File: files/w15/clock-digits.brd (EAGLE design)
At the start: 100 x 80 mm, 6 parts, among them IC1 ATTINY44-SSU, IC2 5V

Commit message: board routing
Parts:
- added R10, R11, R12, R13, R14, R15, R2, R3, R4, R5, R6, R7, R8, R9: (no value), fab:R1206FAB
- added U$10, U$11, U$12, U$13, U$14, U$15, U$16, U$3, U$4, U$5, U$6, U$7, U$8, U$9: LEDFAB1206, fab:LED1206FAB
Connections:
- new net N$1: IC1.13, R2.1, R9.1
- new net N$10: R6.1, U$11.1
- new net N$11: IC1.2, R14.2, R7.2
- new net N$12: R7.1, U$12.1
- new net N$14: R8.1, U$6.1
- new net N$15: IC1.5, R15.2, U$10.2, U$11.2, U$12.2, U$3.2, U$4.2, U$5.2, U$6.2
- new net N$16: R9.2, U$7.1
- new net N$17: R15.1, U$16.1
- new net N$18: R10.1, U$8.1
- new net N$2: R2.2, U$3.1
- new net N$20: R11.1, U$9.1
- new net N$21: R12.1, U$13.1
- new net N$23: R13.1, U$14.1
- new net N$24: R14.1, U$15.1
- new net N$28: IC1.3, R8.2, U$13.2, U$14.2, U$15.2, U$16.2, U$7.2, U$8.2, U$9.2
- new net N$3: IC1.12, R10.2, R3.2
- new net N$4: R3.1, U$4.1
- new net N$5: IC1.11, R11.2, R4.2
- new net N$6: R4.1, U$5.1
- new net N$7: IC1.10, R12.2, R5.2
- new net N$8: R5.1, U$10.1
- new net N$9: IC1.6, R13.2, R6.2
- net SCK: now also IC1.9
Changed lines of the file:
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@@
 <element name="U$1" library="fab" package="2X03SMD" value="AVRISPSMD" x="16.51" y="24.13"/>
 <element name="U$2" library="fab" package="2X02SMD" value="PINHD-2X2-SMD" x="33.02" y="38.1" rot="R180"/>
+<element name="R2" library="fab" package="R1206FAB" value="" x="44.45" y="52.07"/>
+<element name="U$3" library="fab" package="LED1206FAB" value="LEDFAB1206" x="52.07" y="44.45"/>
+<element name="U$4" library="fab" package="LED1206FAB" value="LEDFAB1206" x="57.15" y="38.1" rot="R90"/>
+<element name="U$5" library="fab" package="LED1206FAB" value="LEDFAB1206" x="57.15" y="27.94" rot="R90"/>
+<element name="R3" library="fab" package="R1206FAB" value="" x="53.34" y="49.53"/>
+<element name="R4" library="fab" package="R1206FAB" value="" x="60.96" y="48.26"/>
+<element name="R5" library="fab" package="R1206FAB" value="" x="52.07" y="15.24"/>
+<element name="U$10" library="fab" package="LED1206FAB" value="LEDFAB1206" x="52.07" y="22.86"/>
+<element name="R6" library="fab" package="R1206FAB" value="" x="40.64" y="27.94"/>
+<element name="U$11" library="fab" package="LED1206FAB" value="LEDFAB1206" x="46.99" y="27.94" rot="R90"/>
+<element name="R7" library="fab" package="R1206FAB" value="" x="40.64" y="38.1"/>
+<element name="U$12" library="fab" package="LED1206FAB" value="LEDFAB1206" x="46.99" y="38.1" rot="R90"/>
+<element name="R8" library="fab" package="R1206FAB" value="" x="62.23" y="33.02"/>
+<element name="U$6" library="fab" package="LED1206FAB" value="LEDFAB1206" x="52.07" y="33.02"/>
+<element name="R9" library="fab" package="R1206FAB" value="" x="71.12" y="52.07"/>
+<element name="U$7" library="fab" package="LED1206FAB" value="LEDFAB1206" x="77.47" y="44.45"/>
+<element name="U$8" library="fab" package="LED1206FAB" value="LEDFAB1206" x="82.55" y="38.1" rot="R90"/>
+<element name="U$9" library="fab" package="LED1206FAB" value="LEDFAB1206" x="82.55" y="27.94" rot="R90"/>
+<element name="R10" library="fab" package="R1206FAB" value="" x="81.28" y="49.53"/>
+<element name="R11" library="fab" package="R1206FAB" value="" x="90.17" y="48.26"/>
+<element name="R12" library="fab" package="R1206FAB" value="" x="77.47" y="15.24"/>
+<element name="U$13" library="fab" package="LED1206FAB" value="LEDFAB1206" x="77.47" y="22.86"/>
+<element name="R13" library="fab" package="R1206FAB" value="" x="64.77" y="27.94" rot="R180"/>
+<element name="U$14" library="fab" package="LED1206FAB" value="LEDFAB1206" x="72.39" y="27.94" rot="R90"/>
+<element name="R14" library="fab" package="R1206FAB" value="" x="64.77" y="38.1" rot="R180"/>
+<element name="U$15" library="fab" package="LED1206FAB" value="LEDFAB1206" x="72.39" y="38.1" rot="R90"/>
+<element name="R15" library="fab" package="R1206FAB" value="" x="69.85" y="33.02"/>
+<element name="U$16" library="fab" package="LED1206FAB" value="LEDFAB1206" x="77.47" y="33.02"/>
 </elements>
 <signals>
@@
 <signal name="SCK">
 <contactref element="U$1" pad="3"/>
+<contactref element="IC1" pad="9"/>
+<wire x1="13.97" y1="24.13" x2="33.0835" y2="21.59" width="0" layer="19" extent="1-1"/>
+</signal>
+<signal name="N$2">
+<contactref element="R2" pad="2"/>
+<contactref element="U$3" pad="1"/>
+<wire x1="46.101" y1="52.07" x2="50.419" y2="44.45" width="0" layer="19" extent="1-1"/>
+</signal>
+<signal name="N$3">
+<contactref element="IC1" pad="12"/>
+<contactref element="R3" pad="2"/>
+<contactref element="R10" pad="2"/>
+<wire x1="54.991" y1="49.53" x2="82.931" y2="49.53" width="0" layer="19" extent="1-1"/>
+<wire x1="33.0835" y1="25.4" x2="54.991" y2="49.53" width="0" layer="19" extent="1-1"/>
+</signal>
+<signal name="N$4">
+<contactref element="R3" pad="1"/>
+<contactref element="U$4" pad="1"/>
+<wire x1="57.15" y1="36.449" x2="51.689" y2="49.53" width="0" layer="19" extent="1-1"/>
+</signal>
+<signal name="N$5">
+<contactref element="IC1" pad="11"/>
+<contactref element="R4" pad="2"/>
+<contactref element="R11" pad="2"/>
+<wire x1="62.611" y1="48.26" x2="91.821" y2="48.26" width="0" layer="19" extent="1-1"/>
+<wire x1="33.0835" y1="24.13" x2="62.611" y2="48.26" width="0" layer="19" extent="1-1"/>
+</signal>
+<signal name="N$6">
+<contactref element="R4" pad="1"/>
+<contactref element="U$5" pad="1"/>
+<wire x1="57.15" y1="26.289" x2="59.309" y2="48.26" width="0" layer="19" extent="1-1"/>
+</signal>
+<signal name="N$8">
+<contactref element="R5" pad="1"/>
+<contactref element="U$10" pad="1"/>
+<wire x1="50.419" y1="15.24" x2="50.419" y2="22.86" width="0" layer="19" extent="1-1"/>
+</signal>
+<signal name="N$9">
+<contactref element="IC1" pad="6"/>
+<contactref element="R6" pad="2"/>
+<contactref element="R13" pad="2"/>
+<wire x1="42.291" y1="27.94" x2="63.119" y2="27.94" width="0" layer="19" extent="1-1"/>
+<wire x1="27.8765" y1="21.59" x2="42.291" y2="27.94" width="0" layer="19" extent="1-1"/>
+</signal>
+<signal name="N$10">
+<contactref element="R6" pad="1"/>
+<contactref element="U$11" pad="1"/>
+<wire x1="38.989" y1="27.94" x2="46.99" y2="26.289" width="0" layer="19" extent="1-1"/>
+</signal>
+<signal name="N$12">
+<contactref element="R7" pad="1"/>
+<contactref element="U$12" pad="1"/>
+<wire x1="38.989" y1="38.1" x2="46.99" y2="36.449" width="0" layer="19" extent="1-1"/>
+</signal>
+<signal name="N$14">
+<contactref element="R8" pad="1"/>
+<contactref element="U$6" pad="1"/>
+<wire x1="60.579" y1="33.02" x2="50.419" y2="33.02" width="0" layer="19" extent="1-1"/>
+</signal>
+<signal name="N$1">
+<contactref element="IC1" pad="13"/>
+<contactref element="R2" pad="1"/>
+<contactref element="R9" pad="1"/>
+<wire x1="42.799" y1="52.07" x2="69.469" y2="52.07" width="0" layer="19" extent="1-1"/>
+<wire x1="33.0835" y1="26.67" x2="42.799" y2="52.07" width="0" layer="19" extent="1-1"/>
+</signal>
+<signal name="N$7">
+<contactref element="IC1" pad="10"/>
+<contactref element="R5" pad="2"/>
+<contactref element="R12" pad="2"/>
+<wire x1="53.721" y1="15.24" x2="79.121" y2="15.24" width="0" layer="19" extent="1-1"/>
+<wire x1="33.0835" y1="22.86" x2="53.721" y2="15.24" width="0" layer="19" extent="1-1"/>
+</signal>
+<signal name="N$11">
+<contactref element="IC1" pad="2"/>
+<contactref element="R7" pad="2"/>
+<contactref element="R14" pad="2"/>
+<wire x1="42.291" y1="38.1" x2="63.119" y2="38.1" width="0" layer="19" extent="1-1"/>
+<wire x1="27.8765" y1="26.67" x2="42.291" y2="38.1" width="0" layer="19" extent="1-1"/>
+</signal>
+<signal name="N$15">
+<contactref element="IC1" pad="5"/>
+<contactref element="U$3" pad="2"/>
+<contactref element="U$4" pad="2"/>
+<contactref element="U$5" pad="2"/>
+<contactref element="U$10" pad="2"/>
+<contactref element="U$11" pad="2"/>
+<contactref element="U$12" pad="2"/>
+<contactref element="R15" pad="2"/>
+<contactref element="U$6" pad="2"/>
+<wire x1="53.721" y1="33.02" x2="71.501" y2="33.02" width="0" layer="19" extent="1-1"/>
+<wire x1="46.99" y1="39.751" x2="53.721" y2="33.02" width="0" layer="19" extent="1-1"/>
+<wire x1="46.99" y1="29.591" x2="46.99" y2="39.751" width="0" layer="19" extent="1-1"/>
+<wire x1="53.721" y1="22.86" x2="46.99" y2="29.591" width="0" layer="19" extent="1-1"/>
+<wire x1="57.15" y1="29.591" x2="53.721" y2="22.86" width="0" layer="19" extent="1-1"/>
+<wire x1="57.15" y1="39.751" x2="57.15" y2="29.591" width="0" layer="19" extent="1-1"/>
+<wire x1="53.721" y1="44.45" x2="57.15" y2="39.751" width="0" layer="19" extent="1-1"/>
+<wire x1="27.8765" y1="22.86" x2="53.721" y2="44.45" width="0" layer="19" extent="1-1"/>
+</signal>
+<signal name="N$16">
+<contactref element="R9" pad="2"/>
+<contactref element="U$7" pad="1"/>
+<wire x1="75.819" y1="44.45" x2="72.771" y2="52.07" width="0" layer="19" extent="1-1"/>
+</signal>
+<signal name="N$18">
+<contactref element="R10" pad="1"/>
+<contactref element="U$8" pad="1"/>
+<wire x1="82.55" y1="36.449" x2="79.629" y2="49.53" width="0" layer="19" extent="1-1"/>
+</signal>
+<signal name="N$20">
+<contactref element="R11" pad="1"/>
+<contactref element="U$9" pad="1"/>
+<wire x1="82.55" y1="26.289" x2="88.519" y2="48.26" width="0" layer="19" extent="1-1"/>
+</signal>
+<signal name="N$21">
+<contactref element="R12" pad="1"/>
+<contactref element="U$13" pad="1"/>
+<wire x1="75.819" y1="22.86" x2="75.819" y2="15.24" width="0" layer="19" extent="1-1"/>
+</signal>
+<signal name="N$23">
+<contactref element="R13" pad="1"/>
+<contactref element="U$14" pad="1"/>
+<wire x1="72.39" y1="26.289" x2="66.421" y2="27.94" width="0" layer="19" extent="1-1"/>
+</signal>
+<signal name="N$24">
+<contactref element="R14" pad="1"/>
+<contactref element="U$15" pad="1"/>
+<wire x1="72.39" y1="36.449" x2="66.421" y2="38.1" width="0" layer="19" extent="1-1"/>
+</signal>
+<signal name="N$28">
+<contactref element="U$7" pad="2"/>
+<contactref element="U$8" pad="2"/>
+<contactref element="U$9" pad="2"/>
+<contactref element="U$13" pad="2"/>
+<contactref element="U$14" pad="2"/>
+<contactref element="U$15" pad="2"/>
+<contactref element="U$16" pad="2"/>
+<contactref element="IC1" pad="3"/>
+<contactref element="R8" pad="2"/>
+<wire x1="72.39" y1="29.591" x2="79.121" y2="33.02" width="0" layer="19" extent="1-1"/>
+<wire x1="82.55" y1="29.591" x2="72.39" y2="29.591" width="0" layer="19" extent="1-1"/>
+<wire x1="79.121" y1="44.45" x2="82.55" y2="29.591" width="0" layer="19" extent="1-1"/>
+<wire x1="72.39" y1="39.751" x2="72.39" y2="29.591" width="0" layer="19" extent="1-1"/>
+<wire x1="79.121" y1="22.86" x2="72.39" y2="39.751" width="0" layer="19" extent="1-1"/>
+<wire x1="82.55" y1="39.751" x2="79.121" y2="22.86" width="0" layer="19" extent="1-1"/>
+<wire x1="63.881" y1="33.02" x2="79.121" y2="44.45" width="0" layer="19" extent="1-1"/>
+<wire x1="27.8765" y1="25.4" x2="63.881" y2="33.02" width="0" layer="19" extent="1-1"/>
+</signal>
+<signal name="N$17">
+<contactref element="R15" pad="1"/>
+<contactref element="U$16" pad="1"/>
+<wire x1="75.819" y1="33.02" x2="68.199" y2="33.02" width="0" layer="19" extent="1-1"/>
 </signal>
 </signals>

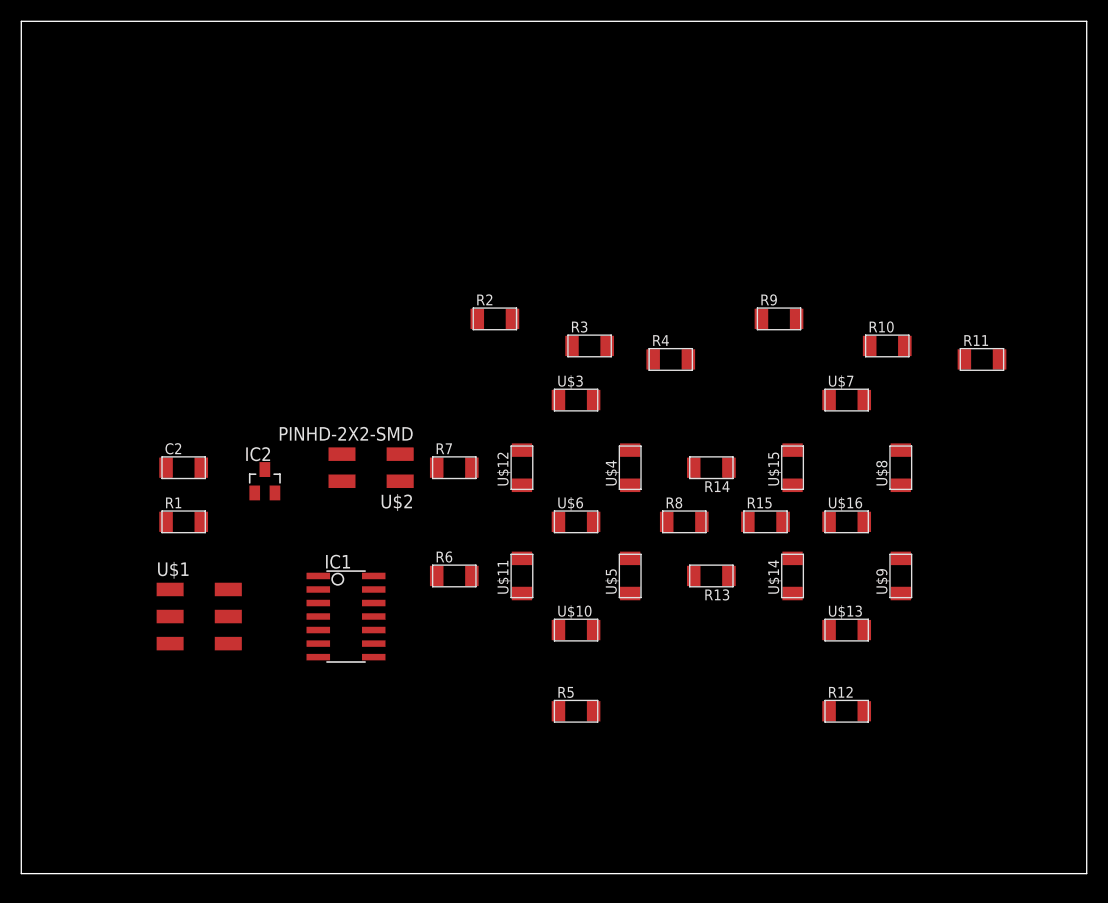
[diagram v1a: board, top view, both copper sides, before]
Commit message: first digit routed internally
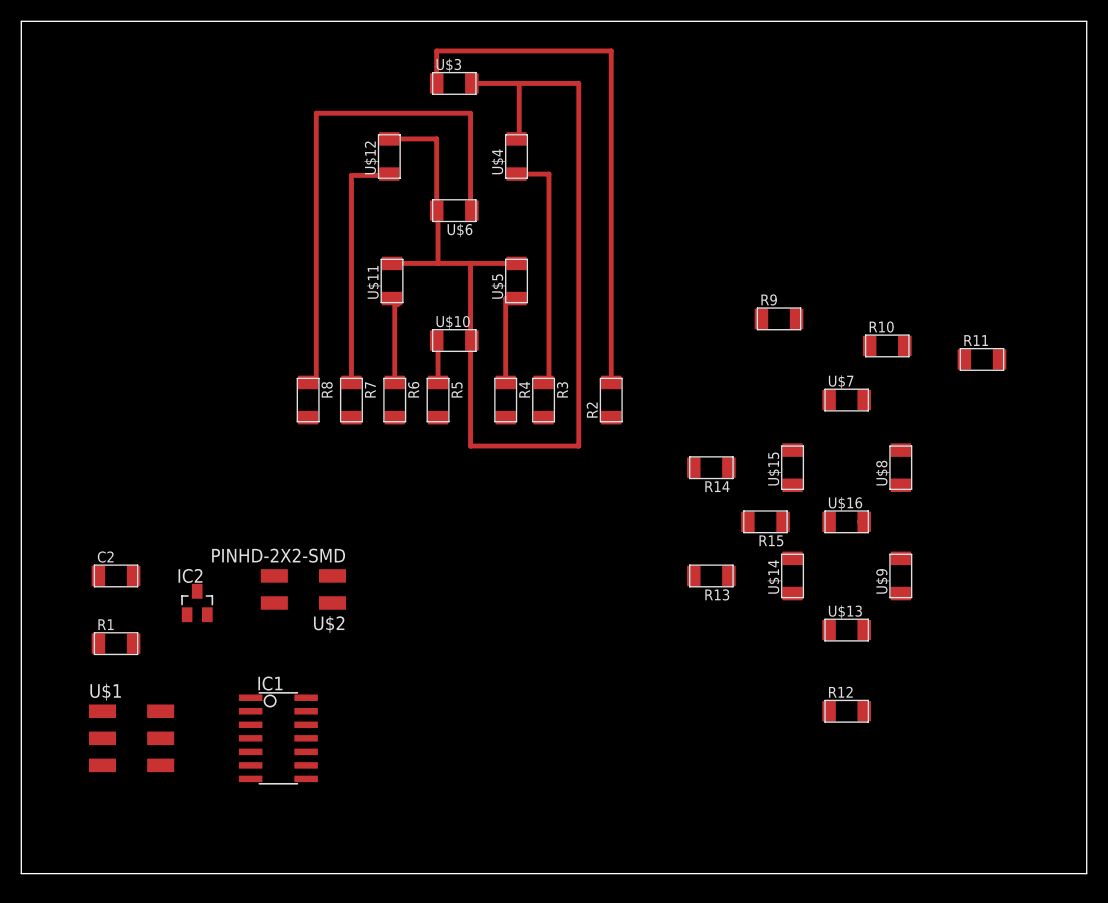
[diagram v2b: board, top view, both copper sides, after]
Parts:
- moved R8 37.1 mm to (26.9, 44.5), turned to 270 degrees
- moved R5 32.0 mm to (39.1, 44.5), turned to 270 degrees
- moved U$3 31.8 mm to (40.6, 74.2)
- moved U$12 31.8 mm to (34.5, 67.3)
- moved U$6 31.4 mm to (40.6, 62.2), turned to 180 degrees
- moved U$4 31.1 mm to (46.5, 67.3)
- moved U$11 30.3 mm to (34.8, 55.6)
- moved U$5 29.7 mm to (46.5, 55.6)
- moved U$10 29.5 mm to (40.6, 50.0)
- moved R6 17.4 mm to (35.1, 44.5), turned to 270 degrees
- moved R4 16.0 mm to (45.5, 44.5), turned to 270 degrees
- moved R2 13.3 mm to (55.4, 44.5), turned to 90 degrees
- moved IC1 13.1 mm to (24.1, 12.7)
- moved R1 13.1 mm to (8.89, 21.6)
- moved U$1 13.1 mm to (10.2, 12.7)
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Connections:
- net VCC: now also C2.1
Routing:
- net N$15: track 0.00 -> 104.9 mm
- net N$2: track 0.00 -> 50.5 mm
- net N$14: track 0.00 -> 49.8 mm
- net N$12: track 0.00 -> 23.5 mm
- net N$4: track 0.00 -> 23.1 mm
- net N$6: track 0.00 -> 9.17 mm
- net N$10: track 0.00 -> 8.34 mm
- net N$8: track 0.00 -> 5.73 mm
- net VIN: track 0.00 -> 1.06 mm

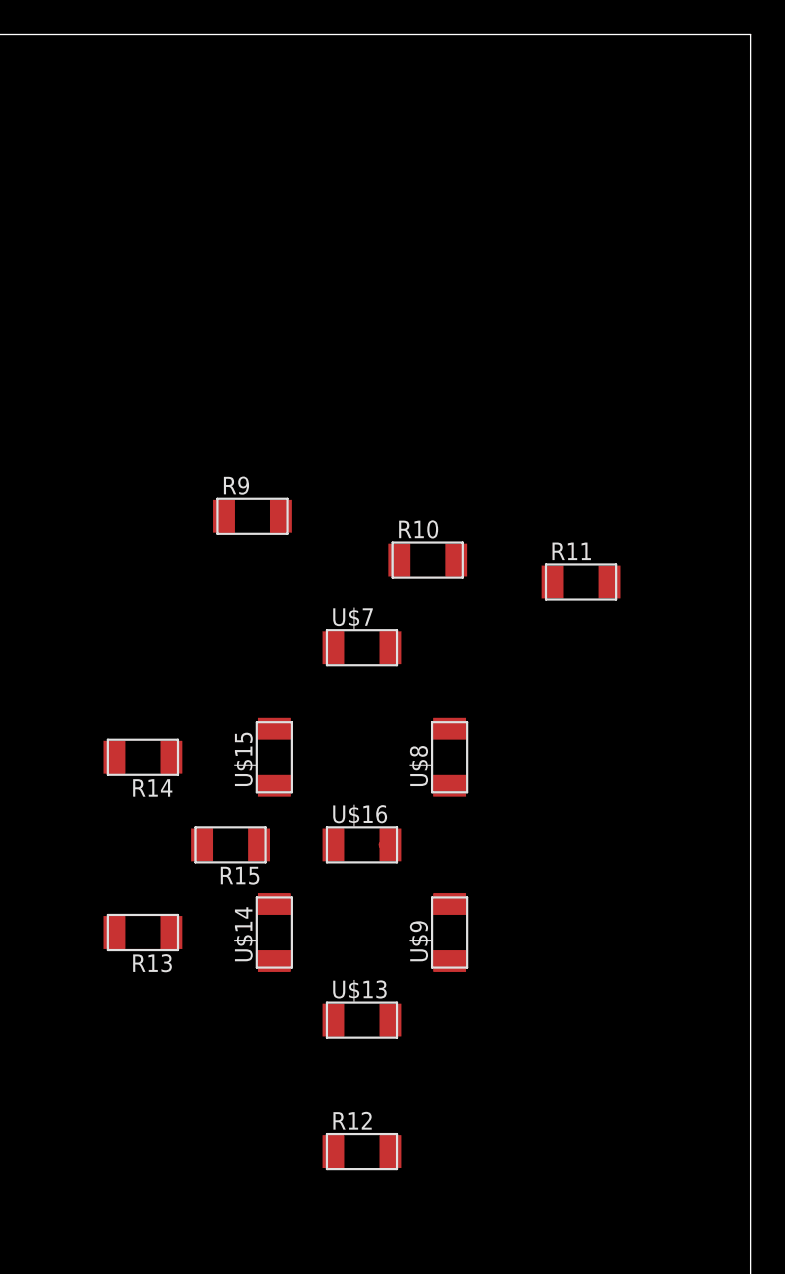
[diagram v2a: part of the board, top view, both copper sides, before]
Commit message: 2nd digit routed
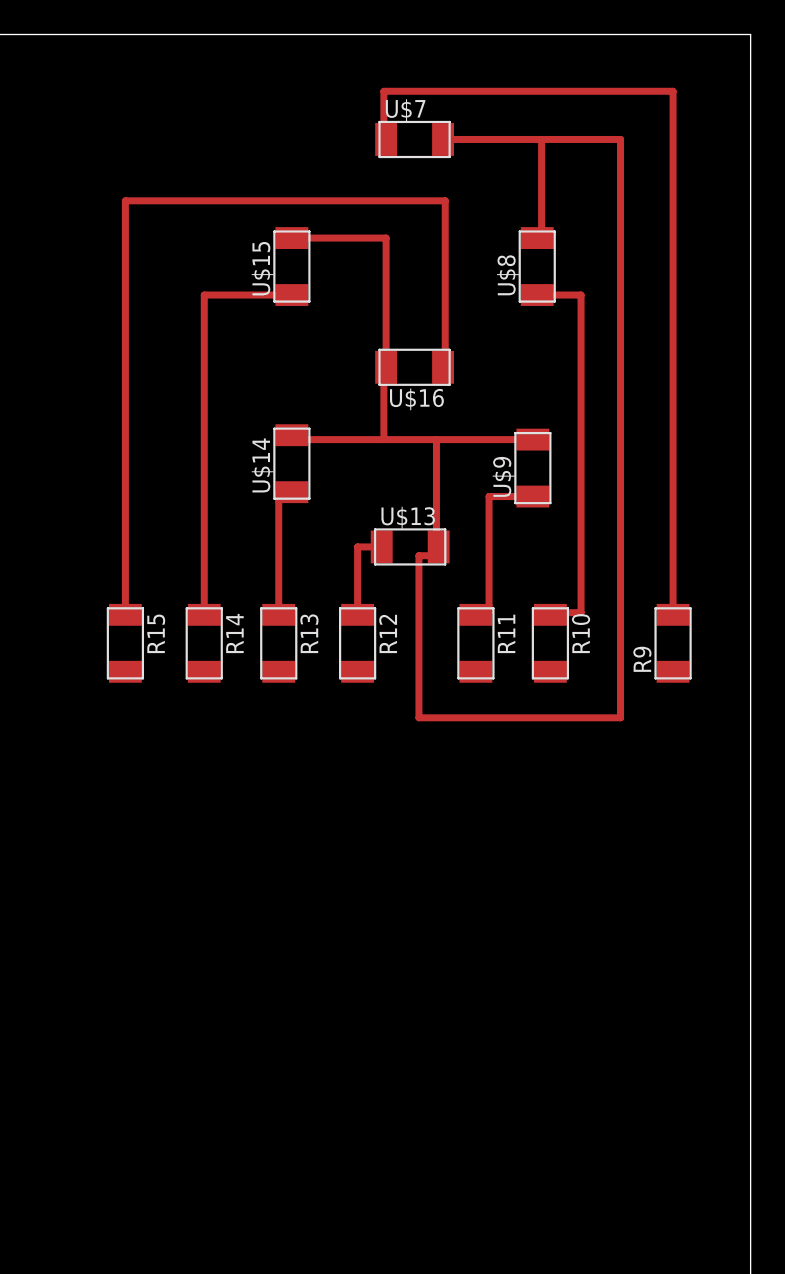
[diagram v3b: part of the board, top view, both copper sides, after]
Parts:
- moved U$7 29.6 mm to (80.5, 73.9)
- moved R12 29.5 mm to (77.2, 44.7), turned to 270 degrees
- moved U$8 28.9 mm to (87.6, 66.5)
- moved U$15 28.5 mm to (73.4, 66.5)
- moved U$16 27.9 mm to (80.5, 60.7), turned to 180 degrees
- moved U$13 27.6 mm to (80.3, 50.3)
- moved U$9 27.4 mm to (87.4, 54.9)
- moved U$14 27.2 mm to (73.4, 55.1)
- moved R9 25.5 mm to (95.5, 44.7), turned to 90 degrees
- moved R13 18.5 mm to (72.6, 44.7), turned to 270 degrees
- moved R15 13.2 mm to (63.8, 44.7), turned to 270 degrees
- moved R10 8.59 mm to (88.4, 44.7), turned to 270 degrees
- moved R14 7.50 mm to (68.3, 44.7), turned to 270 degrees
- moved R11 7.06 mm to (84.1, 44.7), turned to 270 degrees
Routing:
- net N$28: track 0.38 -> 110.4 mm
- net N$17: track 0.00 -> 52.3 mm
- net N$16: track 0.00 -> 50.0 mm
- net N$24: track 0.00 -> 23.6 mm
- net N$18: track 0.00 -> 22.9 mm
- net N$20: track 0.00 -> 10.2 mm
- net N$23: track 0.00 -> 7.87 mm
- net N$21: track 0.00 -> 5.33 mm

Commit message: starting on 7-digit module
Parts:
- moved C2 16.0 mm to (11.4, 12.2), turned to 90 degrees
- moved R1 16.0 mm to (11.4, 5.84), turned to 90 degrees
- moved U$1 13.9 mm to (21.8, 5.08), turned to 270 degrees
- moved R10 8.70 mm to (89.4, 36.1)
- moved R11 8.70 mm to (85.1, 36.1)
- moved R12 8.70 mm to (78.2, 36.1)
- moved R14 8.70 mm to (69.3, 36.1)
- moved R15 8.70 mm to (64.8, 36.1)
- moved U$13 8.70 mm to (81.3, 41.7)
- moved U$16 8.70 mm to (81.5, 52.1)
- moved U$8 8.70 mm to (88.6, 57.9)
- moved R13 8.70 mm to (73.7, 36.1)
- moved R9 8.70 mm to (96.5, 36.1)
- moved U$14 8.70 mm to (74.4, 46.5)
- moved U$15 8.70 mm to (74.4, 57.9)
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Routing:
- net N$1: track 0.00 -> 110.9 mm
- net N$3: track 0.00 -> 106.4 mm
- net N$5: track 0.00 -> 104.6 mm
- net N$7: track 0.00 -> 100.3 mm
- net N$11: track 0.00 -> 91.2 mm
- net N$9: track 0.00 -> 88.4 mm
- net VCC: track 0.00 -> 53.5 mm
- net GND: track 0.00 -> 44.2 mm
- net RST: track 0.00 -> 23.2 mm
- net VIN: track 1.06 -> 19.0 mm
- net SCK: track 0.00 -> 8.95 mm
- net MISO: track 0.00 -> 6.03 mm
